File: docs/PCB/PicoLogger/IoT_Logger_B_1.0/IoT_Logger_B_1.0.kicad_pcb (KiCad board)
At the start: 2 copper layers, 106.1 x 71.8 mm, 129 parts, among them J1 JTAG, J10 Modbus, J2 ESP_UART, J3 USB-C, J4 Sensor, J5 LCD 16x2, J6 Additional, J7 SPI, J8 Relay, J9 CAN, Q1 BSS138, Q2 AO3407, Q3 BC817-40-DIO, SW1 Tact Switch 6x6mm / 13mm, SW2 Tact Switch 6x6mm / 13mm, SW3 Tact Switch 6x6mm / 13mm, SW4 Tact Switch 6x6mm / 13mm, U1 STM32F412RGTx, U2 ESP32-C6-WROOM-1U, U3 AP63200WU, U4 PCA9306DCUR, U5 SN65HVD230DR, U6 MAX3485CSA+, U7 TPD2EUSB30, Y1 3225-25M-SR, Y2 32.768K-CFPX217

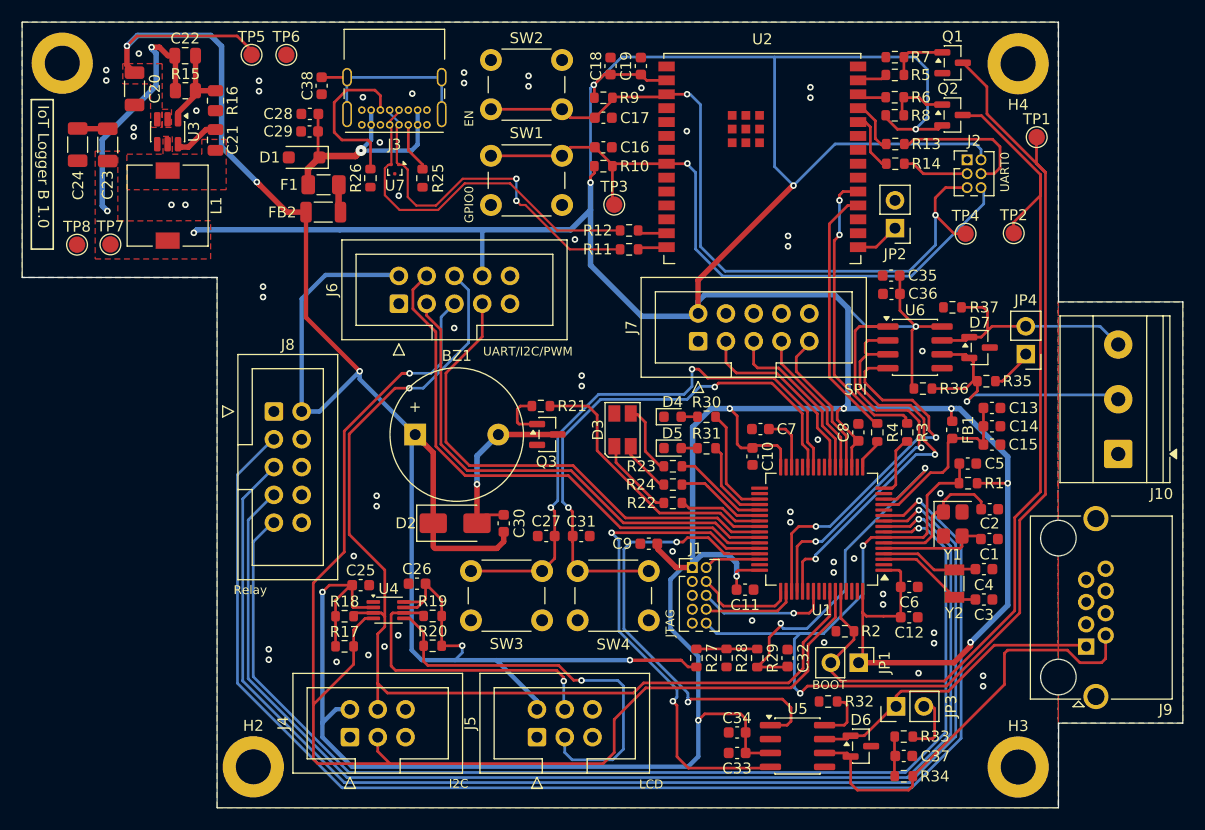
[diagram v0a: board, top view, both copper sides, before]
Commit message: Logger IoT B and C production files generated, backend and frontend prepared for new logger type.
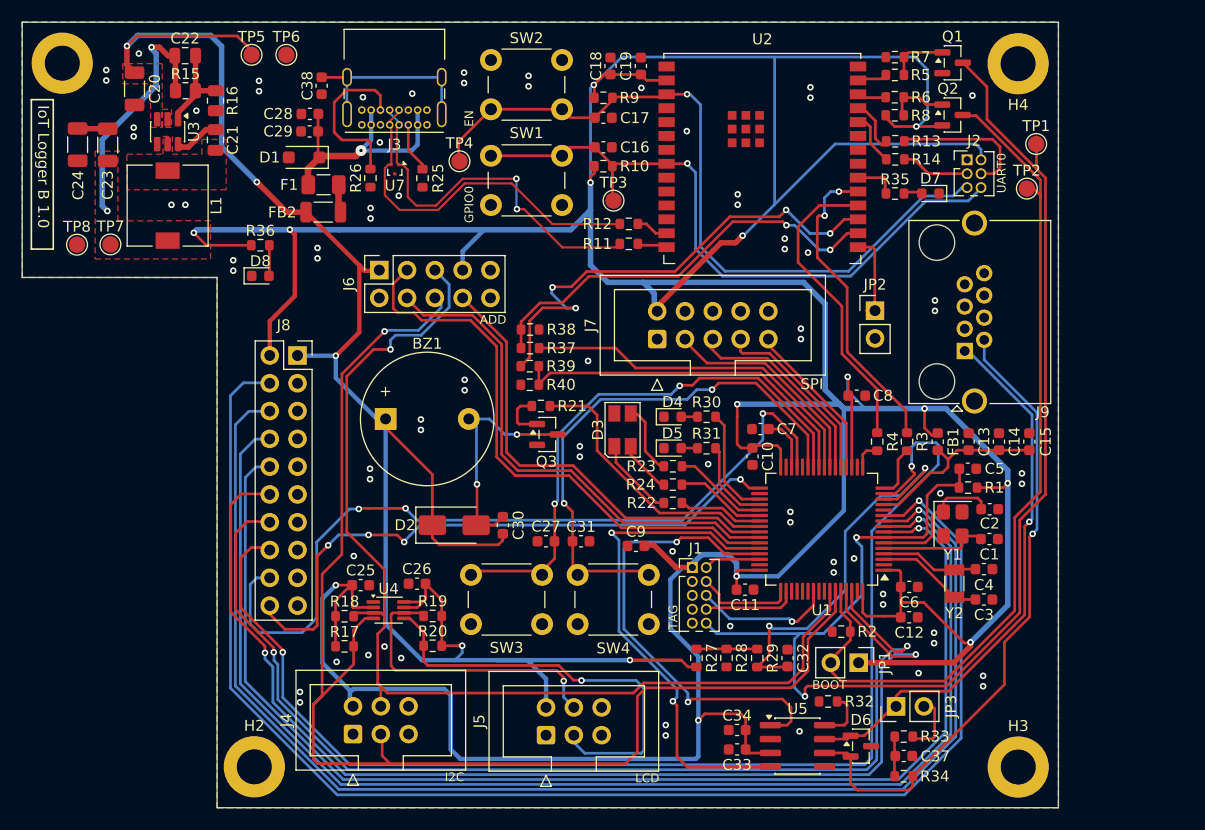
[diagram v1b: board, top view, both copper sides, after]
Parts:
- removed C35: 1uF, Capacitor_SMD:C_0603_1608Metric
- removed C36: 100nF, Capacitor_SMD:C_0603_1608Metric
- removed J10: Modbus, TerminalBlock_Phoenix:TerminalBlock_Phoenix_MKDS-1,5-3_1x03_P5.00mm_Horizontal
- removed JP4: Jumper_2_Bridged, Connector_PinHeader_2.54mm:PinHeader_1x02_P2.54mm_Vertical
- removed U6: MAX3485CSA+, Package_SO:SOIC-8_3.9x4.9mm_P1.27mm
- added D8: LED, LED_SMD:LED_0603_1608Metric, F.Cu at (83.2, 85.6)
- added R38: 100kR, Resistor_SMD:R_0603_1608Metric, F.Cu at (107.9, 90.5)
- added R39: 100R, Resistor_SMD:R_0603_1608Metric, F.Cu at (107.9, 93.9)
- added R40: 100kR, Resistor_SMD:R_0603_1608Metric, F.Cu at (107.9, 95.6)
- D7: value SM712TR-SMC -> LED; footprint Package_TO_SOT_SMD:SOT-23 -> LED_SMD:LED_0603_1608Metric
- J6: footprint Connector_IDC:IDC-Header_2x05_P2.54mm_Vertical -> Connector_PinSocket_2.54mm:PinSocket_2x05_P2.54mm_Vertical
- J8: value Relay -> CON; footprint Connector_IDC:IDC-Header_2x05_P2.54mm_Vertical -> Connector_PinSocket_2.54mm:PinSocket_2x10_P2.54mm_Vertical
- R35: value 120R -> 1kR
- R36: value 680R -> 1kR
- R37: value 680R -> 100R
- moved R36 62.0 mm to (83.2, 82.8), turned to 180 degrees
- moved TP4 46.7 mm to (101.5, 75.2)
- moved R37 38.8 mm to (107.9, 92.2)
- moved J9 29.2 mm to (147.6, 92.5)
- moved R35 19.1 mm to (141.2, 78.1), turned to 180 degrees
- moved D7 14.8 mm to (144.5, 78.1), turned to 180 degrees
- moved JP2 7.75 mm to (139.4, 88.8), turned to 0 degrees
- moved J8 5.56 mm to (86.7, 92.9)
- moved TP2 4.25 mm to (153.3, 77.7)
- moved C13 3.75 mm to (148.0, 100.8), turned to 90 degrees
- moved J7 3.75 mm to (119.5, 91.4)
- moved J6 3.55 mm to (94.1, 85.1)
- moved C15 3.43 mm to (153.5, 100.8), turned to 90 degrees
- moved C8 3.35 mm to (137.8, 96.6), turned to 0 degrees
- moved BZ1 3.06 mm to (94.7, 98.7)
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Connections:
- net CAN2_TX renamed GPIOB13
- D7 pad 1: RS485_B -> GND
- D7 pad 2: RS485_A -> Net-(D7-A)
- J6 pad 1: GND -> +5V
- J6 pad 2: +5V -> GND
- J6 pad 3: USART1_TX -> USART1_RX
- J6 pad 4: USART1_RX -> USART1_TX
- J6 pad 5: I2C1_SDA -> I2C1_SCL
- J6 pad 6: I2C1_SCL -> I2C1_SDA
- J6 pad 7: TIM1_CH1 -> +3.3V
- J6 pad 8: +3.3V -> TIM1_CH1
- J8 pad 1: GND -> +5V
- J8 pad 10: GND -> GPIOC0
- J8 pad 2: +5V -> +3.3V
- J8 pad 3: GPIOC3 -> GND
- J8 pad 4: GND -> GPIOC3
- J8 pad 5: GPIOC2 -> GND
- J8 pad 6: GND -> GPIOC2
- J8 pad 7: GPIOC1 -> GND
- J8 pad 8: GND -> GPIOC1
- J8 pad 9: GPIOC0 -> GND
- R35 pad 1: RS485_A -> Net-(D7-A)
- R35 pad 2: Net-(JP4-A) -> GPIO22
- R36 pad 1: +3.3V -> Net-(D8-A)
- R36 pad 2: RS485_A -> +3.3V
- R37 pad 1: RS485_B -> GPIOC4
- R37 pad 2: GND -> GPIO18
- U1 pad 29: I2C2_SCL -> TIM2_CH3
- U1 pad 33: CAN2_RX -> GPIOB12
- U1 pad 62: I2C2_SDA -> TIM4_CH4
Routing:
- net ADC1_1: track 0.00 -> 114.0 mm, vias 0 -> 2
- net TIM4_CH3: track 0.00 -> 104.7 mm, vias 0 -> 2
- net TIM4_CH4: track 0.00 -> 98.8 mm, vias 0 -> 2
- net TIM2_CH3: track 0.00 -> 74.3 mm, vias 0 -> 3
- net GPIOB12: track 0.00 -> 56.4 mm, vias 0 -> 4
- net GPIO19: track 0.00 -> 45.0 mm, vias 0 -> 4
- net GPIO18: track 0.00 -> 38.7 mm, vias 0 -> 2
- net GPIOC12: track 38.2 -> 0.00 mm, vias 2 -> 0
- net USART3_RX: track 37.2 -> 0.00 mm, vias 2 -> 0
- net USART3_TX: track 34.7 -> 0.00 mm, vias 2 -> 0
- net GPIOC5: track 0.00 -> 33.1 mm
- net GPIOC4: track 0.00 -> 32.6 mm
- net RS485_A: track 25.8 -> 0.00 mm, vias 1 -> 0
- net CANH1: track 28.1 -> 50.7 mm, vias 0 -> 1
- net RS485_B: track 22.0 -> 0.00 mm
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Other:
- board size 106.1 x 71.8 mm -> 94.7 x 71.8 mm
- board text added: "ADD"
- board text removed: "Relay"
- board text removed: "UART/I2C/PWM"

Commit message: IoT_Logger code
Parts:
- moved J9 7.37 mm to (149.5, 85.4), turned to -90 degrees
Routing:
- net CANL1: track 58.7 -> 73.5 mm
- net CANH1: track 50.7 -> 58.3 mm
- net GND: vias 75 -> 76
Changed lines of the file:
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@@
 	(footprint "PersonalLib:RJ45_Amphenol_RJHSE5380_SHORT"
 		(layer "F.Cu")
-		(at 147.62 92.491 90)
+		(at 149.525 85.375 -90)
 		(descr "Shielded, https://www.amphenolcanada.com/ProductSearch/drawings/AC/RJHSE538X.pdf")
 		(tags "RJ45 8p8c ethernet cat5")
@@
 		)
 		(property "Datasheet" "~"
-			(at 0 0 90)
+			(at 0 0 270)
 			(unlocked yes)
 			(layer "F.Fab")
@@
 		)
 		(property "Description" "RJ connector, 8P8C (8 positions 8 connected), RJ31/RJ32/RJ33/RJ34/RJ35/RJ41/RJ45/RJ49/RJ61, Shielded"
-			(at 0 0 90)
+			(at 0 0 270)
 			(unlocked yes)
 			(layer "F.Fab")
@@
 		)
 		(property "Sim.Library" ""
-			(at 0 0 90)
+			(at 0 0 270)
 			(unlocked yes)
 			(layer "F.Fab")
@@
 		(attr through_hole)
 		(fp_line
-			(start 11.925 -5.100278)
-			(end 11.925 -0.5)
+			(start -4.805 7.86)
+			(end -4.805 2.3)
 			(stroke
 				(width 0.12)
@@
 		)
 		(fp_line
-			(start -4.801403 -5.100278)
-			(end 11.838597 -5.100278)
+			(start -4.76 7.86)
+			(end 11.925 7.86)
 			(stroke
 				(width 0.12)
@@
 		)
 		(fp_line
-			(start -4.801403 -5.100278)
-			(end -4.805 -0.5)
+			(start 11.925 7.86)
+			(end 11.925 2.3)
 			(stroke
 				(width 0.12)
@@
 		)
 		(fp_line
-			(start -5.5 -1.2)
-			(end -5 -0.7)
+			(start -5.5 -0.2)
+			(end -5.5 -1.2)
 			(stroke
 				(width 0.12)
@@
 		)
 		(fp_line
-			(start -5.5 -0.2)
-			(end -5.5 -1.2)
+			(start -5.5 -1.2)
+			(end -5 -0.7)
 			(stroke
 				(width 0.12)
@@
 		)
 		(fp_line
-			(start 11.925 7.86)
-			(end 11.925 2.3)
+			(start -4.801403 -5.100278)
+			(end -4.805 -0.5)
 			(stroke
 				(width 0.12)
@@
 		)
 		(fp_line
-			(start -4.76 7.86)
-			(end 11.925 7.86)
+			(start -4.801403 -5.100278)
+			(end 11.838597 -5.100278)
 			(stroke
 				(width 0.12)
@@
 		)
 		(fp_line
-			(start -4.805 7.86)
-			(end -4.805 2.3)
+			(start 11.925 -5.100278)
+			(end 11.925 -0.5)
 			(stroke
 				(width 0.12)
@@
 		)
 		(fp_line
-			(start 13.34 -6)
+			(start -6.22 8.25)
 			(end 13.34 8.25)
 			(stroke
@@
 		(fp_line
 			(start -6.22 -6)
-			(end 13.34 -6)
+			(end -6.22 8.25)
 			(stroke
 				(width 0.05)
@@
 		(fp_line
 			(start -6.22 -6)
-			(end -6.22 8.25)
+			(end 13.34 -6)
 			(stroke
 				(width 0.05)
@@
 		)
 		(fp_line
-			(start -6.22 8.25)
+			(start 13.34 -6)
 			(end 13.34 8.25)
 			(stroke
@@
 		)
 		(fp_line
-			(start 11.815 -5)
+			(start -4.695 7.75)
 			(end 11.815 7.75)
 			(stroke
@@
 		)
 		(fp_line
-			(start -3.755 -5)
-			(end 11.755 -5)
+			(start -4.695 -4.5)
+			(end -4.695 7.75)
 			(stroke
 				(width 0.1)
@@
 		)
 		(fp_line
-			(start -4.695 -4.5)
-			(end -4.695 7.75)
+			(start -3.755 -5)
+			(end 11.755 -5)
 			(stroke
 				(width 0.1)
@@
 		)
 		(fp_line
-			(start -4.695 7.75)
+			(start 11.815 -5)
 			(end 11.815 7.75)
 			(stroke
@@
 		)
 		(pad "" np_thru_hole circle
-			(at -2.79 -2.54 90)
+			(at -2.79 -2.54 270)
 			(size 3.25 3.25)
 			(drill 3.25)
@@
 		)
 		(pad "" np_thru_hole circle
-			(at 9.91 -2.54 90)
+			(at 9.91 -2.54 270)
 			(size 3.25 3.25)
 			(drill 3.25)
@@
 		)
 		(pad "1" thru_hole rect
-			(at 0 0 90)
+			(at 0 0 270)
 			(size 1.5 1.5)
 			(drill 0.89)
@@
 		)
 		(pad "2" thru_hole circle
-			(at 1.016 1.78 90)
+			(at 1.016 1.78 270)
 			(size 1.5 1.5)
 			(drill 0.89)
@@
 		)
 		(pad "3" thru_hole circle
-			(at 2.032 0 90)
+			(at 2.032 0 270)
 			(size 1.5 1.5)
 			(drill 0.89)
@@
 		)
 		(pad "4" thru_hole circle
-			(at 3.048 1.78 90)
+			(at 3.048 1.78 270)
 			(size 1.5 1.5)
 			(drill 0.89)
@@
 		)
 		(pad "5" thru_hole circle
-			(at 4.064 0 90)
+			(at 4.064 0 270)
 			(size 1.5 1.5)
 			(drill 0.89)
@@
 		)
 		(pad "6" thru_hole circle
-			(at 5.08 1.78 90)
+			(at 5.08 1.78 270)
 			(size 1.5 1.5)
 			(drill 0.89)
@@
 		)
 		(pad "7" thru_hole circle
-			(at 6.096 0 90)
+			(at 6.096 0 270)
 			(size 1.5 1.5)
 			(drill 0.89)
@@
 		)
 		(pad "8" thru_hole circle
-			(at 7.112 1.78 90)
+			(at 7.112 1.78 270)
 			(size 1.5 1.5)
 			(drill 0.89)
@@
 		)
 		(pad "SH" thru_hole circle
-			(at -4.57 0.89 90)
+			(at -4.57 0.89 270)
 			(size 2.3 2.3)
 			(drill 1.57)
@@
 		)
 		(pad "SH" thru_hole circle
-			(at 11.69 0.89 90)
+			(at 11.69 0.89 270)
 			(size 2.3 2.3)
 			(drill 1.57)
@@
 	)
 	(via
+		(at 147.725 84.375)
+		(size 0.6)
+		(drill 0.3)
+		(layers "F.Cu" "B.Cu")
+		(free yes)
+		(net 2)
+	)
+	(via
 		(at 93.275 104.2)
 		(size 0.6)
@@
 	)
 	(segment
-		(start 153.775 98.325)
-		(end 147.941 92.491)
+		(start 154.525 88.925)
+		(end 150.975 85.375)
 		(width 0.25)
 		(layer "B.Cu")
@@
 	)
 	(segment
-		(start 153.525 108.1)
-		(end 153.775 107.85)
+		(start 154.525 107.1)
+		(end 154.525 88.925)
 		(width 0.25)
 		(layer "B.Cu")
@@
 	)
 	(segment
-		(start 153.775 107.85)
-		(end 153.775 98.325)
+		(start 150.975 85.375)
+		(end 149.525 85.375)
 		(width 0.25)
 		(layer "B.Cu")
@@
 	)
 	(segment
-		(start 147.941 92.491)
-		(end 147.62 92.491)
+		(start 153.525 108.1)
+		(end 154.525 107.1)
 		(width 0.25)
 		(layer "B.Cu")
@@
 	)
 	(segment
-		(start 154.225 98.125)
-		(end 149.4 93.3)
+		(start 153.825 109.2)
+		(end 154.975 108.05)
 		(width 0.25)
 		(layer "B.Cu")
@@
 	)
 	(segment
-		(start 154.225 108.8)
-		(end 154.225 98.125)
+		(start 146.85 85.496)
+		(end 147.745 86.391)
 		(width 0.25)
 		(layer "B.Cu")
@@
 	)
 	(segment
-		(start 149.4 93.3)
-		(end 149.4 91.475)
+		(start 154.975 108.05)
+		(end 154.975 88.7)
 		(width 0.25)
 		(layer "B.Cu")
@@
 	)
 	(segment
-		(start 153.825 109.2)
-		(end 154.225 108.8)
+		(start 154.975 88.7)
+		(end 149.4 83.125)
+		(width 0.25)
+		(layer "B.Cu")
+		(net 113)
+	)
+	(segment
+		(start 147.5 83.125)
+		(end 146.85 83.775)
+		(width 0.25)
+		(layer "B.Cu")
+		(net 113)
+	)
+	(segment
+		(start 146.85 83.775)
+		(end 146.85 85.496)
 		(width 0.25)
 		(layer "B.Cu")
@@
 	)
 	(segment
+		(start 149.4 83.125)
+		(end 147.5 83.125)
+		(width 0.25)
+		(layer "B.Cu")
+		(net 113)
+	)
+	(segment
+		(start 147.941 92.491)
+		(end 147.62 92.491)
+		(width 0.25)
+		(layer "B.Cu")
+		(net 116)
+	)
+	(segment

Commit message: Code added, documentation review.
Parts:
- added Q4: BSS138, Package_TO_SOT_SMD:SOT-23, F.Cu at (106.3, 105.0)
- added R41: 100kR, Resistor_SMD:R_0603_1608Metric, F.Cu at (111.0, 82.7)
- added R42: 4k7R, Resistor_SMD:R_0603_1608Metric, F.Cu at (111.0, 84.3)
- added R43: 1k, Resistor_SMD:R_0603_1608Metric, F.Cu at (112.2, 104.9)
- added R44: 100k, Resistor_SMD:R_0603_1608Metric, F.Cu at (109.4, 105.0)
- moved R25 1.90 mm to (98.1, 74.8)
- moved R26 1.90 mm to (93.3, 74.8)
- moved U7 1.30 mm to (95.5, 74.6)
- moved TP3 0.60 mm to (115.5, 78.2)
- moved C16 0.58 mm to (114.6, 73.3)
- moved R10 0.57 mm to (114.6, 75.0)
- moved J3 0.55 mm to (98.5, 71.3)
- moved R11 0.55 mm to (117.0, 83.2)
- moved R12 0.55 mm to (116.9, 81.4)
- moved C38 0.40 mm to (88.5, 68.1)
- moved Q3 0.37 mm to (109.5, 99.8)
- moved R21 0.37 mm to (108.9, 97.2)
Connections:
- net JTAG_JTRST renamed GPIOB4
- U2 pad 9: unconnected-(U2-GPIO1/ADC1_CH1/XTAL_32K_N-Pad9) -> GPIO01
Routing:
- net EN: track 68.6 -> 118.3 mm, vias 1 -> 4
- net GPIOB2: track 0.00 -> 37.7 mm, vias 0 -> 2
- net GPIOB13: track 0.00 -> 31.0 mm, vias 0 -> 2
- net GPIO01: track 0.00 -> 21.8 mm
- net Net-(Q4-G): track 0.00 -> 4.96 mm
- net USB_D-: track 33.2 -> 30.6 mm
- net USB_D+: track 34.1 -> 32.4 mm, vias 2 -> 0
- net USB_VBUS: track 23.9 -> 25.3 mm
- net USB_CC2: track 15.2 -> 13.9 mm
- net USB_CC1: track 4.59 -> 3.30 mm
- net +3.3V: track 471.9 -> 471.1 mm
- net TIM2_CH3: track 74.3 -> 74.9 mm
- net GPIOB12: track 56.4 -> 56.9 mm
- net GND: vias 76 -> 78
